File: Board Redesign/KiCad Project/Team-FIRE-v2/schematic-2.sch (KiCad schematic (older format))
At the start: 20 parts, among them J3 UX60-MB-5ST, J4 Conn_01x03, J5 Conn_ARM_JTAG_SWD_10, U4 TXB0108DQSR, U7 TXB0104RUT

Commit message: Finished PCB
- Added various 3D models for a complete 3D visualization of the PCB
- Generated a finalized netlist
- Fixed misnamed net from IR_SIM_RST to IR_SIM_RESET
- Finished all component placement for the PCB; the only work remaining are the mounting holes, and the grounding vias for the IRIDIUM
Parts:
- J3: Height 3.95 -> (none); MPN (none) -> UX60-MB-5ST; Manufacturer (none) -> Hirose; Manufacturer_Name Hirose -> (none); Manufacturer_Part_Number UX60-MB-5ST -> (none); Mouser Part Number 798-UX60-MB-5ST -> (none); Mouser Price/Stock https://www.mouser.co.uk/ProductDetail/Hirose-Connector/UX6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 -> (none); Supplier (none) -> Mouser; Supplier PN (none) -> 798-UX60-MB-5ST
- J4: footprint Connector_PinSocket_2.00mm:PinSocket_1x03_P2.00mm_Horizontal -> Team-FIRE:JST_S3B-PH-SM4-TB(LF)(SN); symbol Connector_Generic:Conn_01x03 -> Connector_Generic_MountingPin:Conn_01x03_MountingPin; Description PA6T voltage pin header -> Voltage pin header
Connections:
- net GND: now also J4.MP (MountPin)
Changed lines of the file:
@@
-$EndComp
-$Comp
-L Connector_Generic:Conn_01x03 J4
-U 1 1 5E58B8FE
-P 2950 3650
-F 0 "J4" V 3050 3700 50  0000 R CNN
-F 1 "Conn_01x03" V 3050 3800 50  0001 R CNN
-F 2 "Connector_PinSocket_2.00mm:PinSocket_1x03_P2.00mm_Horizontal" H 2950 3650 50  0001 C CNN
-F 3 "http://www.jst-mfg.com/product/pdf/eng/ePH.pdf" H 2950 3650 50  0001 C CNN
-F 4 "S3B-PH-SM4-TB(LF)(SN)" V 2950 3650 50  0001 C CNN "MPN"
-F 5 "JST Sales America Inc." V 2950 3650 50  0001 C CNN "Manufacturer"
-F 6 "Digikey" V 2950 3650 50  0001 C CNN "Supplier"
-F 7 "455-1750-1-ND" V 2950 3650 50  0001 C CNN "Supplier PN"
-F 8 "https://www.digikey.com/product-detail/en/jst-sales-america-inc/S3B-PH-SM4-TB-LF-SN/455-1750-1-ND/926847" V 2950 3650 50  0001 C CNN "Link"
-F 9 "100 V" V 2950 3650 50  0001 C CNN "Voltage Rating"
-F 10 "2 A" V 2950 3650 50  0001 C CNN "Current Rating"
-F 11 "PA6T voltage pin header" V 2950 3650 50  0001 C CNN "Description"
-	1    2950 3650
-	1    0    0    -1
 $EndComp
 $Comp
@@
 F 3 "http://www.farnell.com/datasheets/1824852.pdf" H 5200 2350 50  0001 L CNN
 F 4 "USB 2.0" H 5200 2250 50  0001 L CNN "Description"
-F 5 "3.95" H 5200 2150 50  0001 L CNN "Height"
-F 6 "Hirose" H 5200 2050 50  0001 L CNN "Manufacturer_Name"
-F 7 "UX60-MB-5ST" H 5550 2050 50  0001 L CNN "Manufacturer_Part_Number"
-F 8 "798-UX60-MB-5ST" H 5550 1950 50  0001 L CNN "Mouser Part Number"
-F 9 "https://www.mouser.co.uk/ProductDetail/Hirose-Connector/UX60-MB-5ST?qs=XQjbzJWzFPVhtlRA%252Bm3eew%3D%3D" H 5550 1850 50  0001 L CNN "Mouser Price/Stock"
+F 5 "Hirose" H 5200 2050 50  0001 L CNN "Manufacturer"
+F 6 "UX60-MB-5ST" H 5550 2050 50  0001 L CNN "MPN"
+F 7 "798-UX60-MB-5ST" H 5550 1950 50  0001 L CNN "Supplier PN"
+F 8 "Mouser" H 4300 2450 50  0001 C CNN "Supplier"
 	1    4300 2450
 	1    0    0    -1
@@
 Text GLabel 2600 4150 2    39   Input ~ 0
 TES-TX
+$Comp
+L Connector_Generic_MountingPin:Conn_01x03_MountingPin J4
+U 1 1 5E58B8FE
+P 2950 3650
+F 0 "J4" V 3050 3700 50  0000 R CNN
+F 1 "Conn_01x03" V 3050 3800 50  0001 R CNN
+F 2 "Team-FIRE:JST_S3B-PH-SM4-TB(LF)(SN)" H 2950 3650 50  0001 C CNN
+F 3 "http://www.jst-mfg.com/product/pdf/eng/ePH.pdf" H 2950 3650 50  0001 C CNN
+F 4 "S3B-PH-SM4-TB(LF)(SN)" V 2950 3650 50  0001 C CNN "MPN"
+F 5 "JST Sales America Inc." V 2950 3650 50  0001 C CNN "Manufacturer"
+F 6 "Digikey" V 2950 3650 50  0001 C CNN "Supplier"
+F 7 "455-1750-1-ND" V 2950 3650 50  0001 C CNN "Supplier PN"
+F 8 "https://www.digikey.com/product-detail/en/jst-sales-america-inc/S3B-PH-SM4-TB-LF-SN/455-1750-1-ND/926847" V 2950 3650 50  0001 C CNN "Link"
+F 9 "100 V" V 2950 3650 50  0001 C CNN "Voltage Rating"
+F 10 "2 A" V 2950 3650 50  0001 C CNN "Current Rating"
+F 11 "Voltage pin header" V 2950 3650 50  0001 C CNN "Description"
+	1    2950 3650
+	1    0    0    -1
+$EndComp
+$Comp
+L power:GND #PWR0105
+U 1 1 5ED1910A
+P 2950 3950
+F 0 "#PWR0105" H 2950 3700 50  0001 C CNN
+F 1 "GND" H 3200 3900 50  0000 R CNN
+F 2 "" H 2950 3950 50  0001 C CNN
+F 3 "" H 2950 3950 50  0001 C CNN
+	1    2950 3950
+	1    0    0    -1
+$EndComp
 $EndSCHEMATC

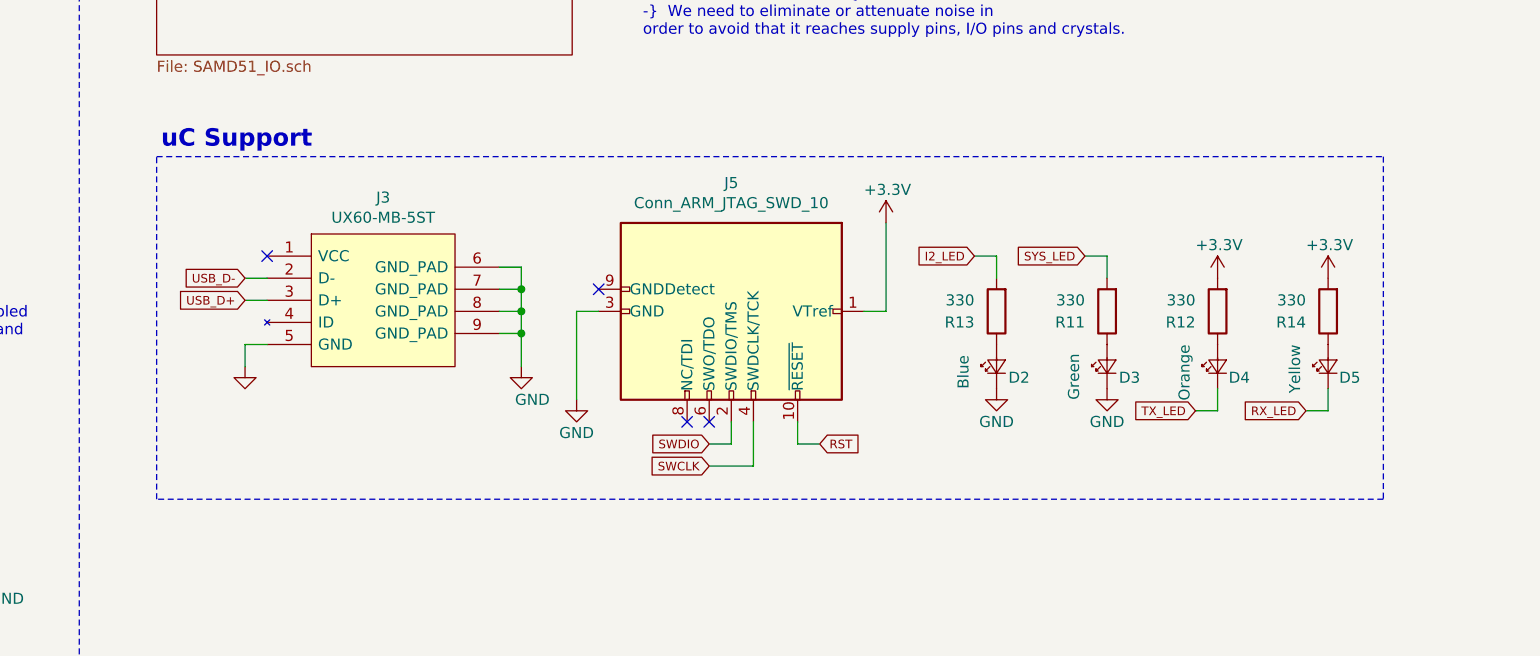
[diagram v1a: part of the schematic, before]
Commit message: Deleted unused LED's, finished mounting for IRIDIUM
- Delete the two unused LEDs from schematic and layout
- Added grounding vias for antenna connection
- Added grounding vias for IRIDIUM 9523 modem
- Added keepout zones (except GND) for antenna and modem
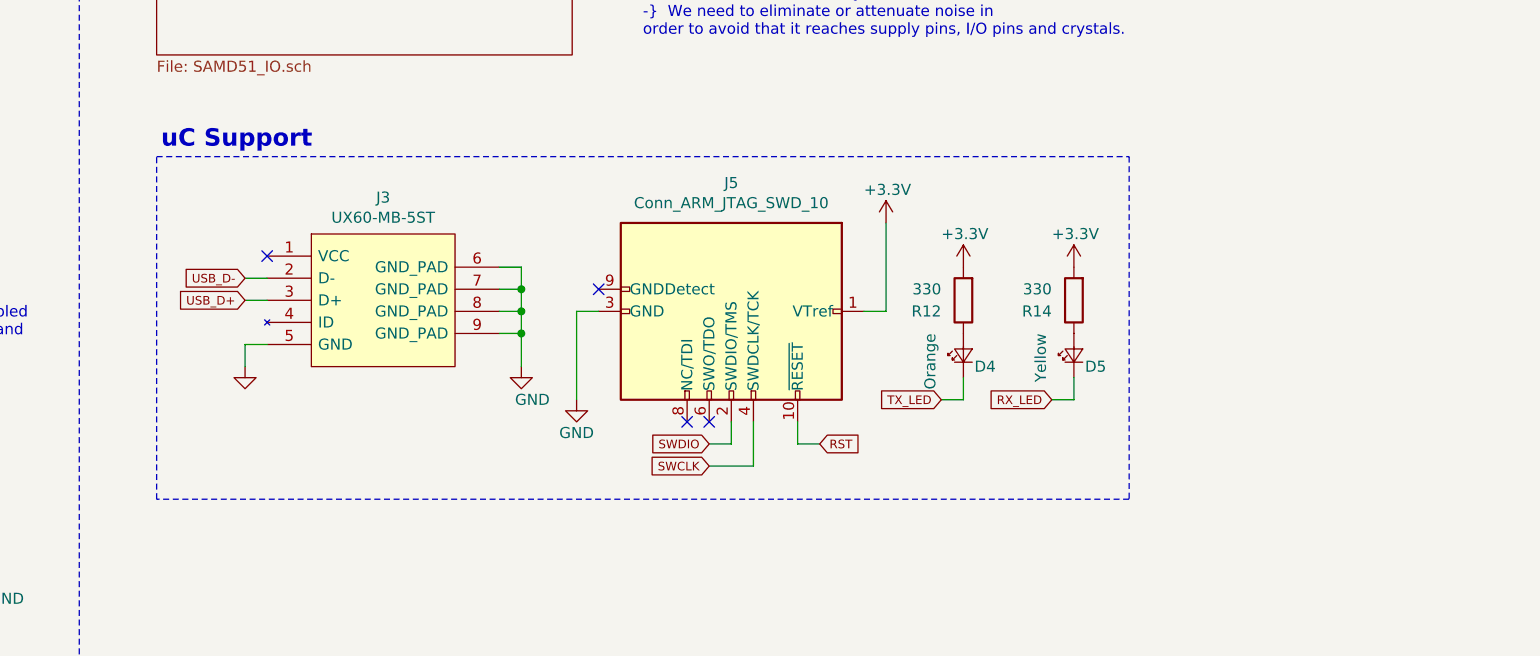
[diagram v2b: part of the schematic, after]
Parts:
- removed D2: Blue, LED_SMD:LED_0603_1608Metric, symbol Device:LED_Small
- removed D3: Green, LED_SMD:LED_0603_1608Metric, symbol Device:LED_Small
- removed R11, R13: 330, Resistor_SMD:R_0603_1608Metric, symbol Device:R
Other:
- moved on the sheet: D4, D5, R12, R14
